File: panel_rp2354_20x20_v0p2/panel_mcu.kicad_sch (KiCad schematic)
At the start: 32 parts, among them SW1 SW_Push, SW2 SW_Push, U1 APS6404L-3SQR, U2 RP2354B_80QFN, Y1 ABM8-272-T3

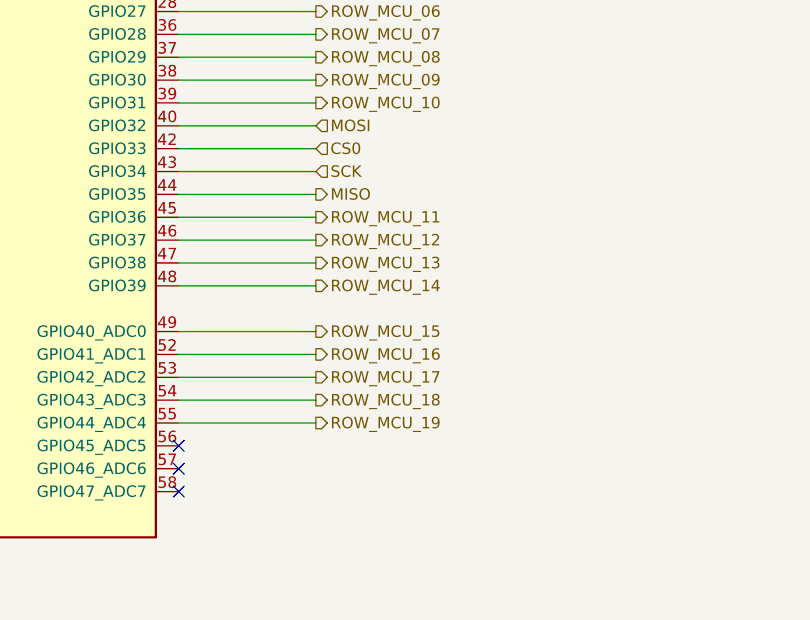
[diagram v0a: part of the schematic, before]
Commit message: Route EINT and add MISO resistor
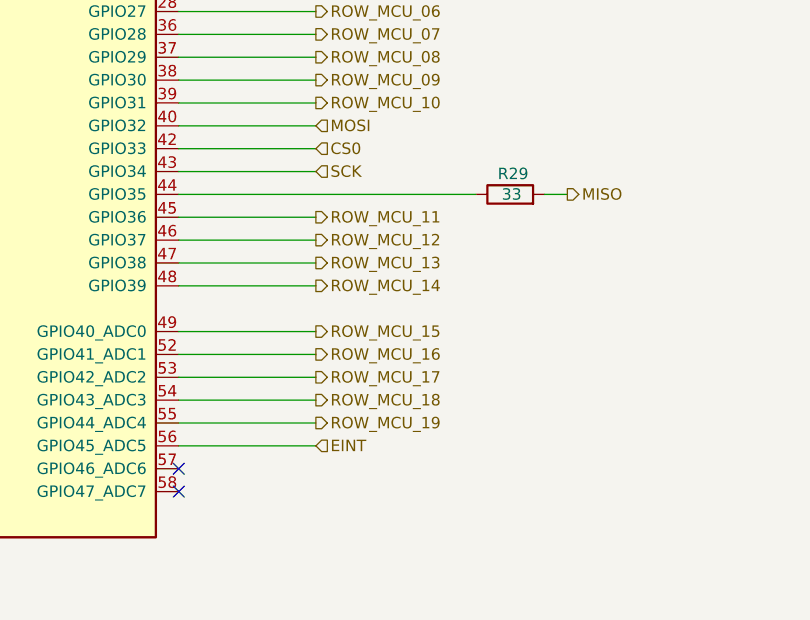
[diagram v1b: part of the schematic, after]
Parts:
- added R29: 33, panel_custom:R_0201_0603Metric, symbol Device:R
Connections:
- net MISO: now also R29.2; no longer U2.44 (GPIO35)
- net EINT: now reaches U2.56 (GPIO45_ADC5)
- new net: R29.1, U2.44 (GPIO35)
- no-connect marks 5 -> 4
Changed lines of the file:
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@@
 		(at 172.72 149.86)
 	)
-	(no_connect
-		(at 241.3 199.39)
-	)
 	(wire
 		(pts
@@
 	(wire
 		(pts
+			(xy 281.94 171.45) (xy 284.48 171.45)
+		)
+		(stroke
+			(width 0)
+			(type default)
+		)
+	)
+	(wire
+		(pts
 			(xy 262.89 260.35) (xy 262.89 262.89)
 		)
@@
 	(wire
 		(pts
-			(xy 241.3 171.45) (xy 256.54 171.45)
+			(xy 241.3 171.45) (xy 274.32 171.45)
 		)
 		(stroke
@@
 	(wire
 		(pts
+			(xy 241.3 199.39) (xy 256.54 199.39)
+		)
+		(stroke
+			(width 0)
+			(type default)
+		)
+	)
+	(wire
+		(pts
 			(xy 172.72 81.28) (xy 148.59 81.28)
 		)
@@
 	(hierarchical_label "MISO"
 		(shape output)
-		(at 256.54 171.45 0)
+		(at 284.48 171.45 0)
+		(effects
+			(font
+				(size 1.27 1.27)
+			)
+			(justify left)
+		)
+	)
+	(hierarchical_label "EINT"
+		(shape input)
+		(at 256.54 199.39 0)
 		(effects
 			(font
@@
 					(unit 1)
 				)
+			)
+		)
+	)
+	(symbol
+		(lib_id "Device:R")
+		(at 278.13 171.45 90)
+		(unit 1)
+		(exclude_from_sim no)
+		(in_bom yes)
+		(on_board yes)
+		(dnp no)
+		(property "Reference" "R29"
+			(at 280.162 169.164 90)
+			(effects
+				(font
+					(size 1.27 1.27)
+				)
+				(justify left)
+			)
+		)
+		(property "Value" "33"
+			(at 279.4 171.45 90)
+			(effects
+				(font
+					(size 1.27 1.27)
+				)
+				(justify left)
+			)
+		)
+		(property "Footprint" "panel_custom:R_0201_0603Metric"
+			(at 278.13 173.228 90)
+			(effects
+				(font
+					(size 1.27 1.27)
+				)
+				(hide yes)
+			)
+		)
+		(property "Datasheet" "~"
+			(at 278.13 171.45 0)
+			(effects
+				(font
+					(size 1.27 1.27)
+				)
+				(hide yes)
+			)
+		)
+		(property "Description" ""
+			(at 278.13 171.45 0)
+			(effects
+				(font
+					(size 1.27 1.27)
+				)
+				(hide yes)
+			)
+		)
+		(property "LCSC Part #" "C295794"
+			(at 278.13 171.45 0)
+			(effects
+				(font
+					(size 1.27 1.27)
+				)
+				(hide yes)
+			)
+		)
+		(pin "1"
+		)
+		(pin "2"
+		)
+		(instances
+			(project "panel_rp2354_20x20"
+				(path "/1e634561-32a0-4ffa-9d4f-e93f355464d5/b30b56c6-21ca-46ed-bb1a-e5062fd43ea8"
+					(reference "R29")
+					(unit 1)
+				)
